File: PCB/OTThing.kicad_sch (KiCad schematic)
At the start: 60 parts, among them IC2 TPS61041, J3 USB_C_Receptacle_USB2.0, Q1 BC847, Q1 BC858, Q2 BC847, Q4 BC858, Q5 BC858, Q7 BC858, SW1 RST/CONFIG, U1 ESP32-WROOM-32, U2 AMS1117-3.3, U3 CH340C, U3 LTV-356T, U4 LTV-356T

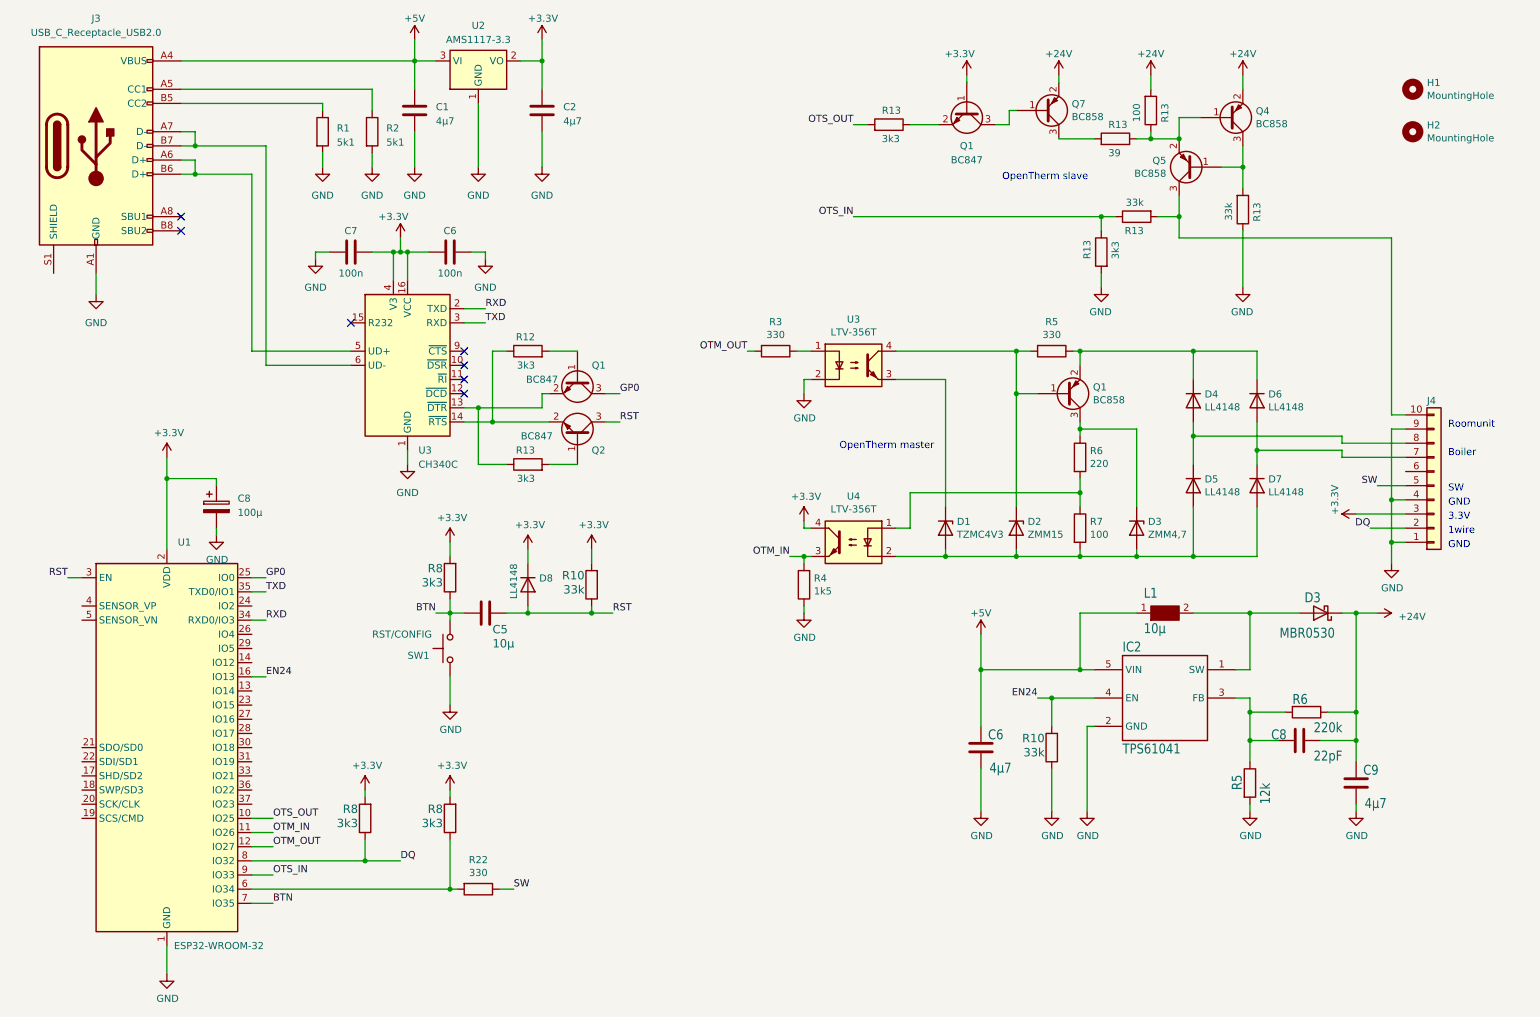
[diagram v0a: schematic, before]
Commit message: change MCU redesign OT interfaces
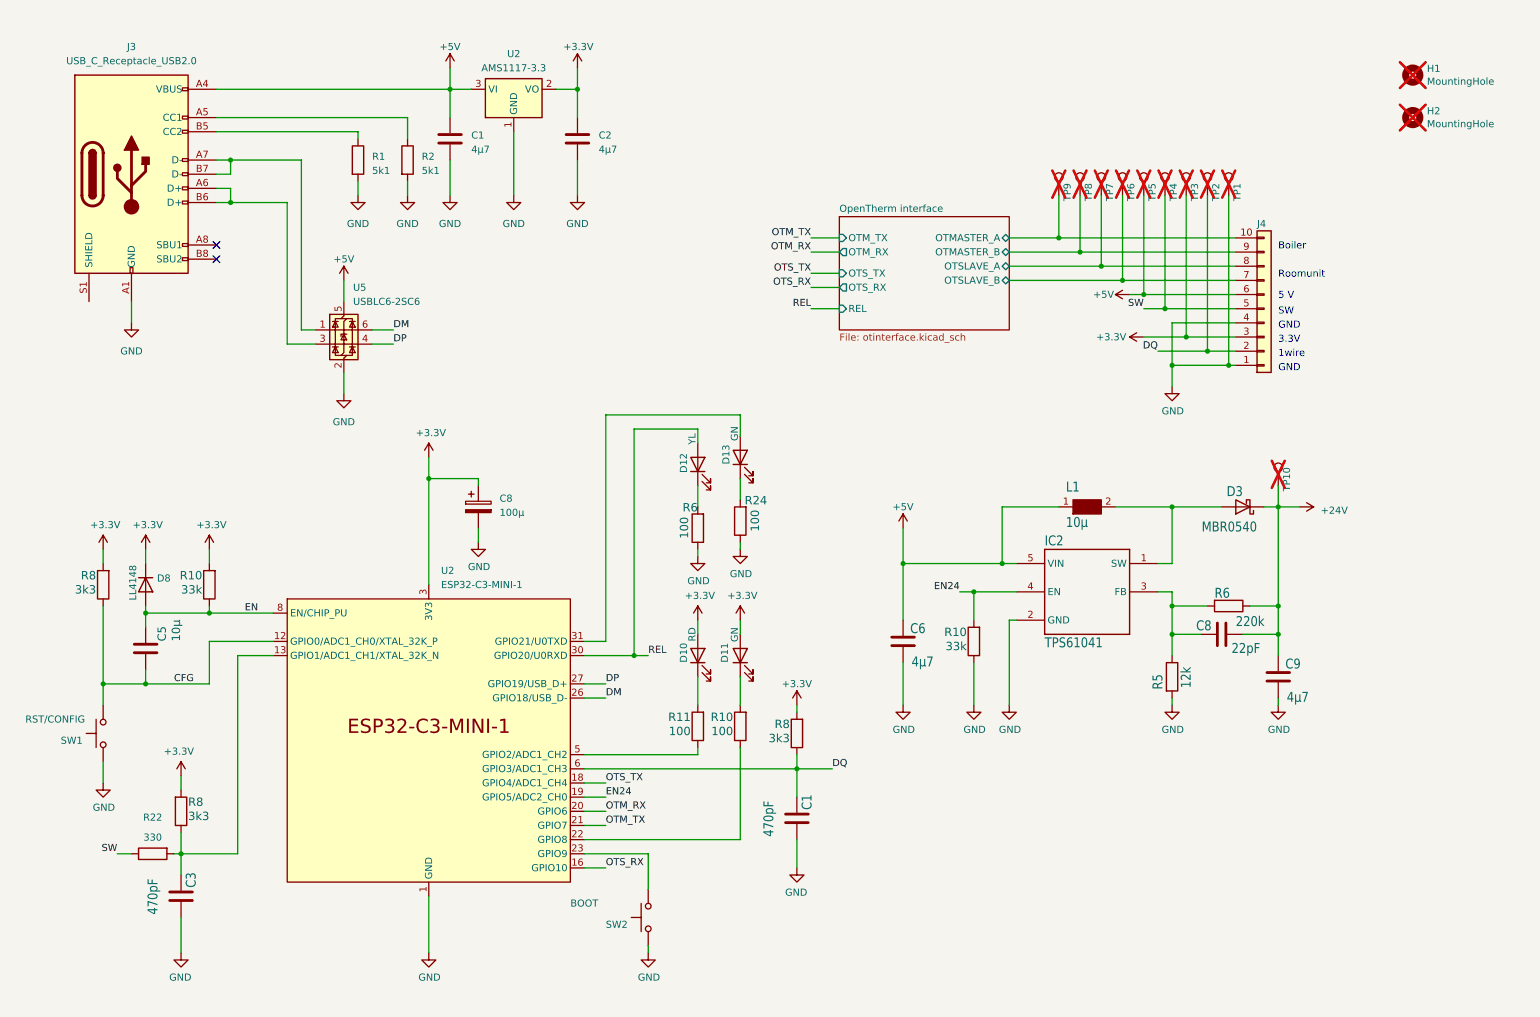
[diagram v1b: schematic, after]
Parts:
- removed C6, C7: 100n, Capacitor_SMD:C_0805_2012Metric, symbol Device:C
- removed D1: TZMC4V3, Diode_SMD:D_MiniMELF, symbol Diode:ZMMxx
- removed D2: ZMM15, Diode_SMD:D_MiniMELF, symbol Diode:ZMMxx
- removed D3: ZMM4,7, Diode_SMD:D_MiniMELF, symbol Diode:ZMMxx
- removed D4, D5, D6, D7: LL4148, Diode_SMD:D_MiniMELF, symbol Diode:LL4148
- removed Q1, Q4, Q5, Q7: BC858, Package_TO_SOT_SMD:SOT-23, symbol Transistor_BJT:BC858
- removed Q1 (x2), Q2: BC847, Package_TO_SOT_SMD:SOT-23, symbol Transistor_BJT:BC847
- removed R12, R13 (x3): 3k3, Resistor_SMD:R_0805_2012Metric, symbol Device:R
- removed R13, R7: 100, Resistor_SMD:R_0805_2012Metric, symbol Device:R
- removed R13 (x2): 33k, Resistor_SMD:R_0805_2012Metric, symbol Device:R
- removed R13: 39, Resistor_SMD:R_0805_2012Metric, symbol Device:R
- removed R3, R5: 330, Resistor_SMD:R_0805_2012Metric, symbol Device:R
- removed R4: 1k5, Resistor_SMD:R_0805_2012Metric, symbol Device:R
- removed U1: ESP32-WROOM-32, RF_Module:ESP32-WROOM-32, symbol RF_Module:ESP32-WROOM-32
- removed U3, U4: LTV-356T, Package_SO:SO-4_4.4x3.6mm_P2.54mm, symbol Isolator:LTV-356T
- removed U3: CH340C, Package_SO:SOIC-16_3.9x9.9mm_P1.27mm, symbol Interface_USB:CH340C
- added C1, C3: 470pF, Capacitor_SMD:C_0805_2012Metric, symbol Device:C
- added D10: RD, LED_SMD:LED_0805_2012Metric, symbol Device:LED
- added D11, D13: GN, LED_SMD:LED_0805_2012Metric, symbol Device:LED
- added D12: YL, LED_SMD:LED_0805_2012Metric, symbol Device:LED
- added R10, R11, R24: 100, Resistor_SMD:R_0805_2012Metric, symbol Device:R
- added SW2: BOOT, Button_Switch_SMD:SW_SPST_CK_RS282G05A3, symbol Switch:SW_Push
- added TP1, TP10, TP2, TP3, TP4, TP5, TP6, TP7, TP8, TP9: ~, TestPoint:TestPoint_THTPad_D1.5mm_Drill0.7mm, symbol Connector:TestPoint
- added U2: ESP32-C3-MINI-1, User:ESP32-C3-MINI-1, symbol espressif:ESP32-C3-MINI-1
- added U5: USBLC6-2SC6, Package_TO_SOT_SMD:SOT-23-6, symbol Power_Protection:USBLC6-2SC6
- C1, C2: LCSC (none) -> C2918489; LCSC order # C319192 -> (none)
- C5: LCSC (none) -> C90543; LCSC order # C15850 -> (none)
- C6, C9: LCSC (none) -> C2918489; LCSC order # C1779 -> (none)
- C8: LCSC (none) -> C2887276; LCSC order # C59937 -> (none)
- C8: LCSC (none) -> C24658; LCSC order # C1804 -> (none)
- D3: value MBR0530 -> MBR0540; LCSC (none) -> C116159; LCSC order # C86299 -> (none)
- D8: LCSC (none) -> C435829; LCSC order # C9808 -> (none)
- H1, H2: now not fitted
- IC2: LCSC (none) -> C9846; LCSC order # C9846 -> (none)
- J3: LCSC (none) -> C2765186
- J4: LCSC (none) -> C5184956
- L1: LCSC (none) -> C2041531; LCSC order # C45403 -> (none)
- R1, R2: LCSC (none) -> C118848; LCSC order # C431925 -> (none)
- R10: LCSC (none) -> C17633; LCSC order # C17633 -> (none)
- R22: LCSC (none) -> C17630
- R5: LCSC (none) -> C17444; LCSC order # C4382 -> (none)
- R6: value 220 -> 100; LCSC (none) -> C17408
- R6: LCSC (none) -> C17556; LCSC order # C149504 -> (none)
- R8: LCSC (none) -> C26010; LCSC order # C114531 -> (none)
- SW1: LCSC (none) -> C2837540; LCSC order # C2837545 -> (none)
- U2: LCSC (none) -> C347222; LCSC order # C351784 -> (none)
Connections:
- net +24V: now also TP10.1
- net +3.3V: now also D10.2 (A), D11.2 (A), TP3.1, U2.3 (3V3)
- net +5V: now also J4.6 (Pin_6), TP5.1, U5.5 (VBUS)
- net DQ: now also C1.1, TP2.1, U2.6 (GPIO3/ADC1_CH3)
- net EN24: now also U2.19 (GPIO5/ADC2_CH0)
- net GND: now also R6.1, C1.2, C3.2, R24.1, SW2.2, TP1.1, U2.1 (GND), U2.11 (GND), U2.14 (GND), U2.2 (GND), U2.36 (GND), U2.37 (GND), U2.38 (GND), U2.39 (GND), U2.40 (GND), U2.41 (GND), U2.42 (GND), U2.43 (GND), U2.44 (GND), U2.45 (GND), U2.46 (GND), U2.47 (GND), U2.48 (GND), U2.49 (GND), U2.50 (GND), U2.51 (GND), U2.52 (GND), U2.53 (GND), U5.2 (GND); no longer J4.9 (Pin_9)
- net SW: now also TP4.1
- net at R6.2: now also D12.1 (K)
- net OpenTherm interface/OTSLAVE_A: now reaches J4.8 (Pin_8)
- net OpenTherm interface/OTSLAVE_A: now also TP7.1
- net OpenTherm interface/OTSLAVE_B: now reaches J4.7 (Pin_7)
- net OpenTherm interface/OTSLAVE_B: now also TP6.1
- net at J3.A6 (D+), J3.B6 (D+): now also U5.3 (I/O2)
- net at J3.A7 (D-), J3.B7 (D-): now also U5.1 (I/O1)
- net OpenTherm interface/OTMASTER_A: now reaches J4.10 (Pin_10)
- net OpenTherm interface/OTMASTER_A: now also TP9.1
- net at R22.2, R8.1: now also C3.1, U2.13 (GPIO1/ADC1_CH1/XTAL_32K_N)
- net BTN renamed CFG
- net CFG: now also U2.12 (GPIO0/ADC1_CH0/XTAL_32K_P)
- net RST renamed EN
- net EN: now also U2.8 (EN/CHIP_PU)
- new net: D11.1 (K), R10.2
- new net: R11.1, U2.5 (GPIO2/ADC1_CH2)
- new net: D10.1 (K), R11.2
- new net: R10.1, U2.22 (GPIO8)
- new net: SW2.1, U2.23 (GPIO9)
- new net: D13.2 (A), U2.31 (GPIO21/U0TXD)
- new net: D13.1 (K), R24.2
- new net DM: U2.26 (GPIO18/USB_D-), U5.6 (I/O1)
- new net DP: U2.27 (GPIO19/USB_D+), U5.4 (I/O2)
- new net OTM_RX: U2.20 (GPIO6)
- new net OTM_TX: U2.21 (GPIO7)
- new net OTS_RX: U2.16 (GPIO10)
- new net OTS_TX: U2.18 (GPIO4/ADC1_CH4)
- new net OpenTherm interface/OTMASTER_B: J4.9 (Pin_9), TP8.1
- new net REL: D12.2 (A), U2.30 (GPIO20/U0RXD)
- no-connect marks 7 -> 2
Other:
- added sheet OpenTherm interface (otinterface.kicad_sch)
- note added: "5 V"
- note removed: "OpenTherm master"
- note removed: "OpenTherm slave"
- moved on the sheet: C1, C2, C5, C6, C8, C9, D3, D8, IC2, J3, J4, L1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

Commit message: Change MCU
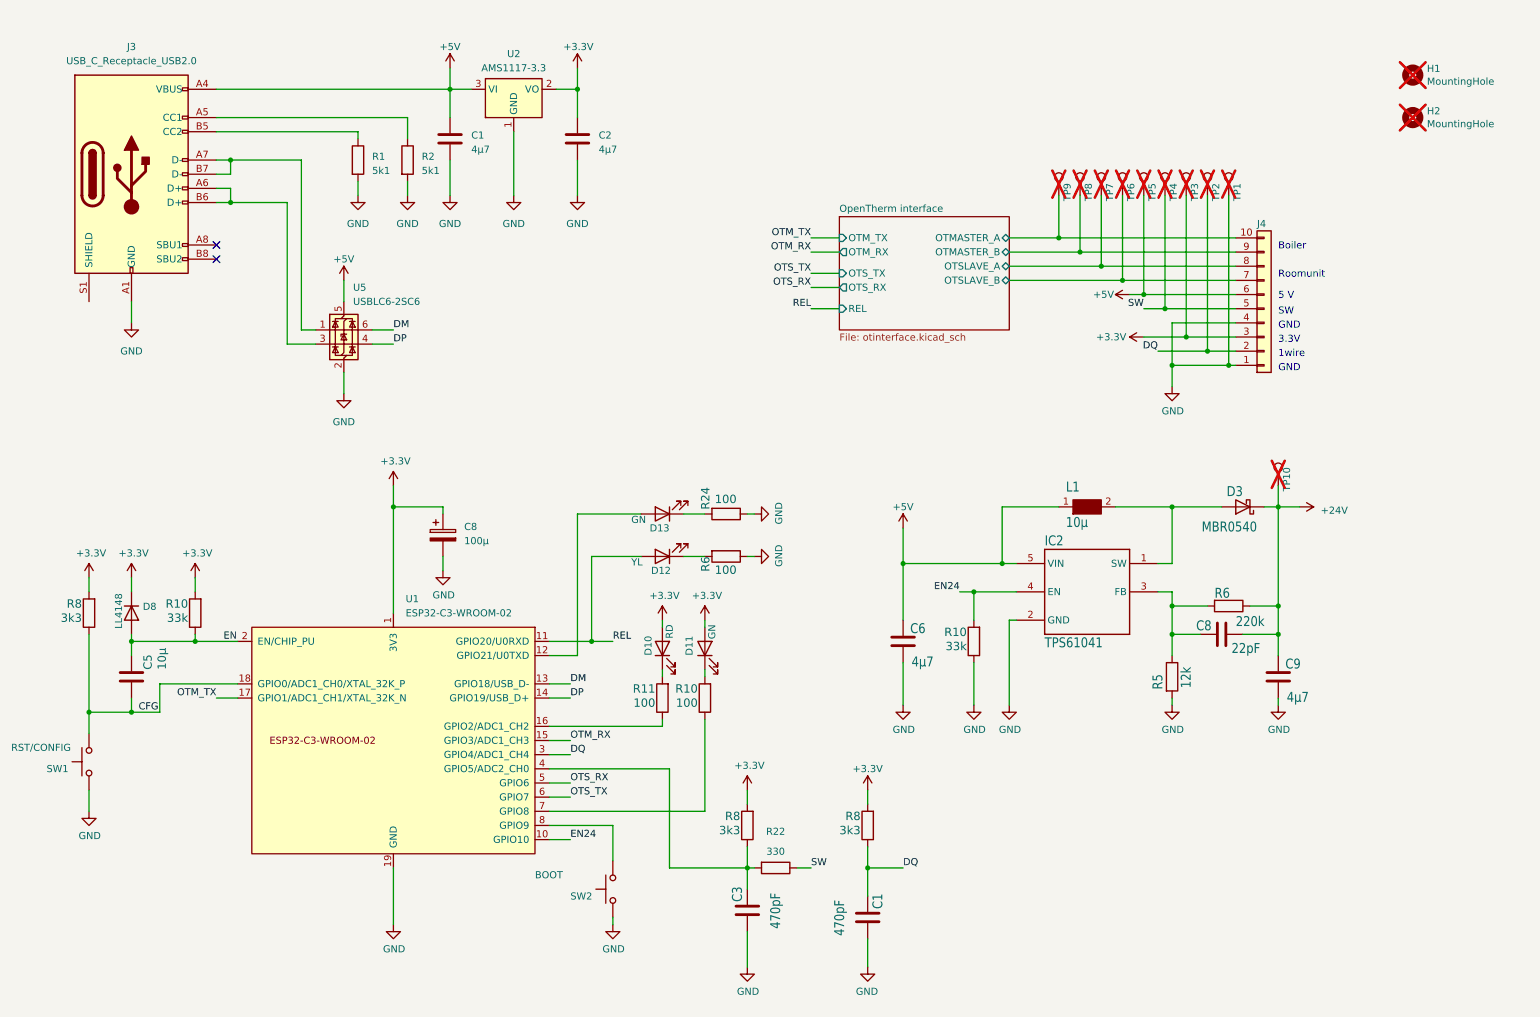
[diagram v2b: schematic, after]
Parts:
- removed U2: ESP32-C3-MINI-1, User:ESP32-C3-MINI-1, symbol espressif:ESP32-C3-MINI-1
- added U1: ESP32-C3-WROOM-02, User:ESP32-C3-WROOM-02, symbol espressif:ESP32-C3-WROOM-02
- J3: LCSC C2765186 -> (none)
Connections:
- net +3.3V: now also U1.1 (3V3)
- net CFG: now also U1.18 (GPIO0/ADC1_CH0/XTAL_32K_P)
- net DM: now also U1.13 (GPIO18/USB_D-)
- net DP: now also U1.14 (GPIO19/USB_D+)
- net DQ: now also U1.3 (GPIO4/ADC1_CH4)
- net EN: now also U1.2 (EN/CHIP_PU)
- net EN24: now also U1.10 (GPIO10)
- net GND: now also U1.19 (GND), U1.9 (GND)
- net OTM_RX: now also U1.15 (GPIO3/ADC1_CH3)
- net OTM_TX: now also U1.17 (GPIO1/ADC1_CH1/XTAL_32K_N)
- net OTS_RX: now also U1.5 (GPIO6)
- net OTS_TX: now also U1.6 (GPIO7)
- net REL: now also U1.11 (GPIO20/U0RXD)
- net at C3.1, R22.2, R8.1: now also U1.4 (GPIO5/ADC2_CH0)
- net at R11.1: now also U1.16 (GPIO2/ADC1_CH2)
- net at R10.1: now also U1.7 (GPIO8)
- net at SW2.1: now also U1.8 (GPIO9)
- net at D13.2 (A): now also U1.12 (GPIO21/U0TXD)
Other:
- moved on the sheet: C1, C3, C5, C8, D10, D11, D12, D13, D8, R10, R11, R22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

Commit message: finish 45/24
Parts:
- J3: LCSC (none) -> C2927038
- L1: LCSC C2041531 -> C98020
- U1: LCSC (none) -> C2934560
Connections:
- net GND: now also D13.1 (K); no longer R24.1
- net at R24.2: now also U1.12 (GPIO21/U0TXD); no longer D13.1 (K)
- net at D13.2 (A): now also R24.1; no longer U1.12 (GPIO21/U0TXD)
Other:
- moved on the sheet: D13, R24
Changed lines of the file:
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@@
 	(symbol
 		(lib_id "Device:R")
-		(at 140.97 105.41 270)
+		(at 129.54 105.41 270)
 		(unit 1)
 		(exclude_from_sim no)
@@
 		(dnp no)
 		(property "Reference" "R24"
-			(at 136.398 100.584 0)
+			(at 124.968 100.584 0)
 			(effects
 				(font
@@
 		)
 		(property "Value" "100"
-			(at 138.938 103.632 90)
+			(at 127.508 103.632 90)
 			(effects
 				(font
@@
 		)
 		(property "Footprint" "Resistor_SMD:R_0805_2012Metric"
-			(at 140.97 103.632 90)
+			(at 129.54 103.632 90)
 			(effects
 				(font
@@
 		)
 		(property "Datasheet" "~"
-			(at 140.97 105.41 0)
+			(at 129.54 105.41 0)
 			(effects
 				(font
@@
 		)
 		(property "Description" ""
-			(at 140.97 105.41 0)
+			(at 129.54 105.41 0)
 			(effects
 				(font
@@
 		)
 		(property "LCSC" "C17408"
-			(at 140.97 105.41 0)
+			(at 129.54 105.41 0)
 			(effects
 				(font
@@
 			)
 		)
-		(property "LCSC" ""
+		(property "LCSC" "C2927038"
 			(at 34.29 44.45 0)
 			(effects
@@
 			)
 		)
+		(property "LCSC" "C2934560"
+			(at 81.28 146.05 0)
+			(effects
+				(font
+					(size 1.27 1.27)
+				)
+				(hide yes)
+			)
+		)
 		(pin "2"
 		)
@@
 	(symbol
 		(lib_id "Device:LED")
-		(at 129.54 105.41 180)
+		(at 140.97 105.41 180)
 		(unit 1)
 		(exclude_from_sim no)
@@
 		(dnp no)
 		(property "Reference" "D13"
-			(at 127.254 107.95 0)
+			(at 138.684 107.95 0)
 			(effects
 				(font
@@
 		)
 		(property "Value" "GN"
-			(at 123.952 106.426 0)
+			(at 135.382 106.426 0)
 			(effects
 				(font
@@
 		)
 		(property "Footprint" "LED_SMD:LED_0805_2012Metric"
-			(at 129.54 105.41 0)
+			(at 140.97 105.41 0)
 			(effects
 				(font
@@
 		)
 		(property "Datasheet" "~"
-			(at 129.54 105.41 0)
+			(at 140.97 105.41 0)
 			(effects
 				(font
@@
 		)
 		(property "Description" "Light emitting diode"
-			(at 129.54 105.41 0)
+			(at 140.97 105.41 0)
 			(effects
 				(font
@@
 		)
 		(property "LCSC" "C965847"
-			(at 129.54 105.41 0)
+			(at 140.97 105.41 0)
 			(effects
 				(font
@@
 			)
 		)
-		(property "LCSC" "C2041531"
+		(property "LCSC" "C98020"
 			(at 205.74 106.68 0)
 			(effects

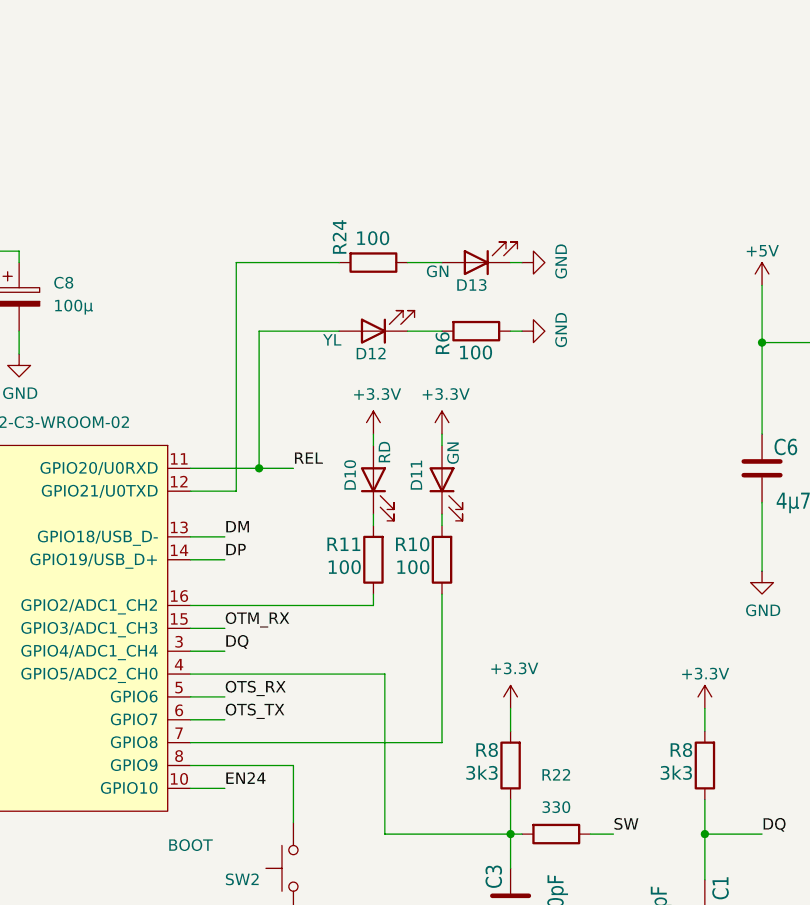
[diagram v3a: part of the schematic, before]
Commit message: add pullups for stability
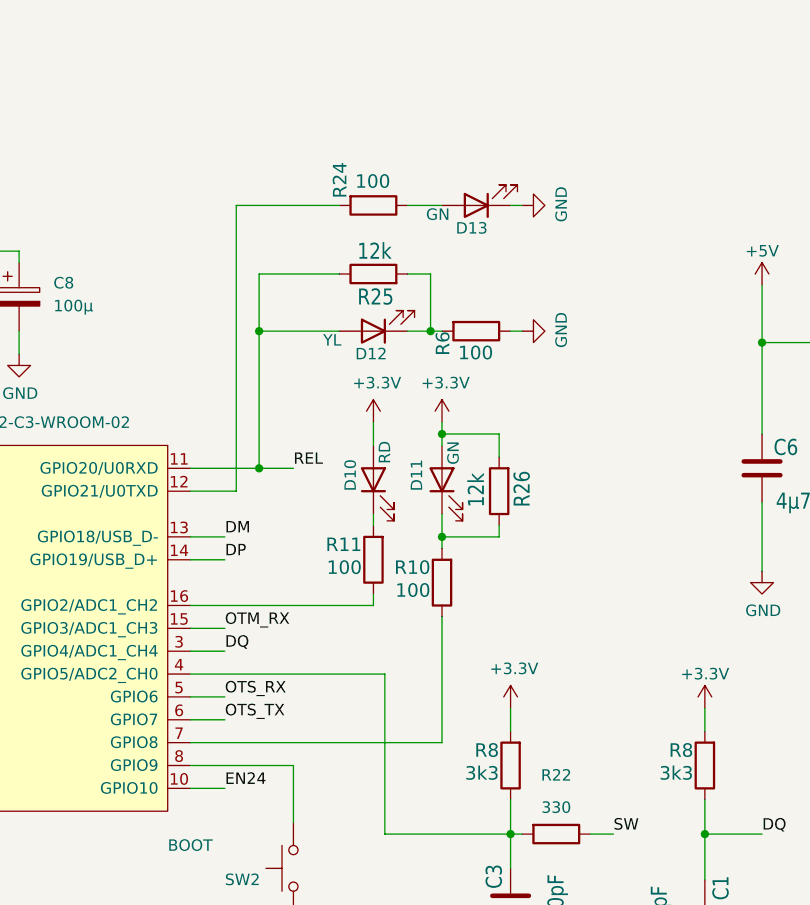
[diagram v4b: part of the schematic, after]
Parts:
- added R25, R26: 12k, Resistor_SMD:R_0805_2012Metric, symbol Device:R
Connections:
- net +3.3V: now also R26.2
- net REL: now also R25.1
- net at D11.1 (K), R10.2: now also R26.1
- net at D12.1 (K), R6.2: now also R25.2
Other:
- company: (none) -> Seegel Systeme
- title: (none) -> OT Thing
- moved on the sheet: D13, R10, R24
